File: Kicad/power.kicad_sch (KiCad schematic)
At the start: 22 parts, among them J6 350543-1, J7 22112042

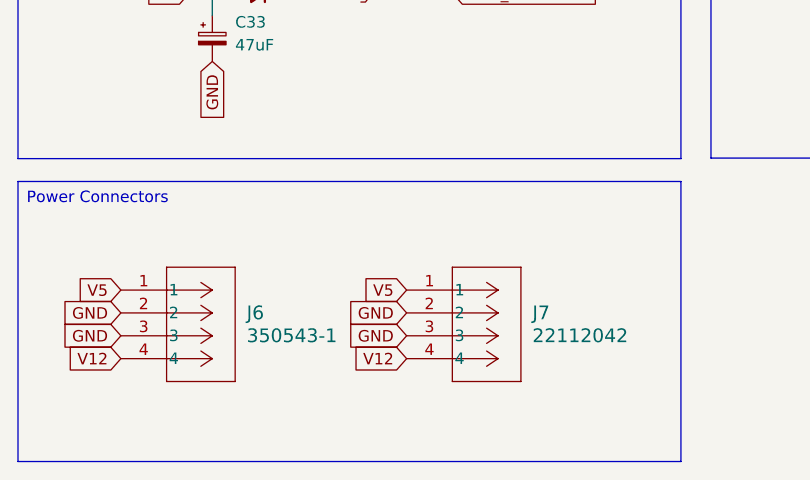
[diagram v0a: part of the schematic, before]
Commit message: Remove large Molex power connector
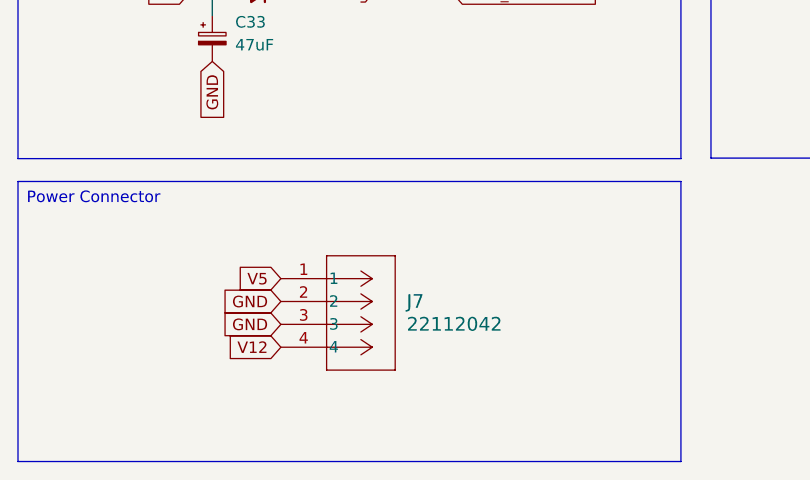
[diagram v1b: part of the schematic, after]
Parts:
- removed J6: 350543-1, 350543_1:CONN_350543-1_TYC, symbol 350543_1:350543-1
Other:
- moved on the sheet: J7
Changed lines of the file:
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@@
 		)
 	)
-	(text_box "Power Connectors\n"
+	(text_box "Power Connector\n"
 		(exclude_from_sim no)
 		(at 21.59 100.965 0)
@@
 		)
 	)
-	(global_label "V12"
-		(shape input)
-		(at 33.02 120.65 180)
-		(fields_autoplaced yes)
-		(effects
-			(font
-				(size 1.27 1.27)
-			)
-			(justify right)
-		)
-		(property "Intersheetrefs" "${INTERSHEET_REFS}"
-			(at 26.5272 120.65 0)
-			(effects
-				(font
-					(size 1.27 1.27)
-				)
-				(justify right)
-				(hide yes)
-			)
-		)
-	)
 	(global_label "GND"
 		(shape input)
@@
 	(global_label "V5"
 		(shape input)
-		(at 33.02 113.03 180)
-		(fields_autoplaced yes)
-		(effects
-			(font
-				(size 1.27 1.27)
-			)
-			(justify right)
-		)
-		(property "Intersheetrefs" "${INTERSHEET_REFS}"
-			(at 27.7367 113.03 0)
-			(effects
-				(font
-					(size 1.27 1.27)
-				)
-				(justify right)
-				(hide yes)
-			)
-		)
-	)
-	(global_label "V5"
-		(shape input)
 		(at 115.57 35.56 90)
 		(fields_autoplaced yes)
@@
 	(global_label "V5"
 		(shape input)
-		(at 64.77 113.03 180)
+		(at 50.8 111.76 180)
 		(fields_autoplaced yes)
 		(effects
@@
 		)
 		(property "Intersheetrefs" "${INTERSHEET_REFS}"
-			(at 59.4867 113.03 0)
+			(at 45.5167 111.76 0)
 			(effects
 				(font
@@
 	(global_label "GND"
 		(shape input)
-		(at 33.02 115.57 180)
-		(fields_autoplaced yes)
-		(effects
-			(font
-				(size 1.27 1.27)
-			)
-			(justify right)
-		)
-		(property "Intersheetrefs" "${INTERSHEET_REFS}"
-			(at 26.1643 115.57 0)
-			(effects
-				(font
-					(size 1.27 1.27)
-				)
-				(justify right)
-				(hide yes)
-			)
-		)
-	)
-	(global_label "GND"
-		(shape input)
 		(at 104.14 43.18 270)
 		(fields_autoplaced yes)
@@
 		(property "Intersheetrefs" "${INTERSHEET_REFS}"
 			(at 104.14 50.0357 90)
-			(effects
-				(font
-					(size 1.27 1.27)
-				)
-				(justify right)
-				(hide yes)
-			)
-		)
-	)
-	(global_label "GND"
-		(shape input)
-		(at 33.02 118.11 180)
-		(fields_autoplaced yes)
-		(effects
-			(font
-				(size 1.27 1.27)
-			)
-			(justify right)
-		)
-		(property "Intersheetrefs" "${INTERSHEET_REFS}"
-			(at 26.1643 118.11 0)
 			(effects
 				(font
@@
 	(global_label "GND"
 		(shape input)
-		(at 64.77 115.57 180)
+		(at 50.8 114.3 180)
 		(fields_autoplaced yes)
 		(effects
@@
 		)
 		(property "Intersheetrefs" "${INTERSHEET_REFS}"
-			(at 57.9143 115.57 0)
+			(at 43.9443 114.3 0)
 			(effects
 				(font
@@
 	(global_label "GND"
 		(shape input)
-		(at 64.77 118.11 180)
+		(at 50.8 116.84 180)
 		(fields_autoplaced yes)
 		(effects
@@
 		)
 		(property "Intersheetrefs" "${INTERSHEET_REFS}"
-			(at 57.9143 118.11 0)
+			(at 43.9443 116.84 0)
 			(effects
 				(font
@@
 	(global_label "V12"
 		(shape input)
-		(at 64.77 120.65 180)
+		(at 50.8 119.38 180)
 		(fields_autoplaced yes)
 		(effects
@@
 		)
 		(property "Intersheetrefs" "${INTERSHEET_REFS}"
-			(at 58.2772 120.65 0)
+			(at 44.3072 119.38 0)
 			(effects
 				(font
@@
 	)
 	(symbol
-		(lib_id "350543_1:350543-1")
-		(at 33.02 113.03 0)
-		(unit 1)
-		(exclude_from_sim no)
-		(in_bom yes)
-		(on_board yes)
-		(dnp no)
-		(fields_autoplaced yes)
-		(property "Reference" "J6"
-			(at 46.99 115.5699 0)
-			(effects
-				(font
-					(size 1.524 1.524)
-				)
-				(justify left)
-			)
-		)
-		(property "Value" "350543-1"
-			(at 46.99 118.1099 0)
-			(effects
-				(font
-					(size 1.524 1.524)
-				)
-				(justify left)
-			)
-		)
-		(property "Footprint" "350543_1:CONN_350543-1_TYC"
-			(at 33.02 113.03 0)
-			(effects
-				(font
-					(size 1.27 1.27)
-					(italic yes)
-				)
-				(hide yes)
-			)
-		)
-		(property "Datasheet" "350543-1"
-			(at 33.02 113.03 0)
-			(effects
-				(font
-					(size 1.27 1.27)
-					(italic yes)
-				)
-				(hide yes)
-			)
-		)
-		(property "Description" ""
-			(at 33.02 113.03 0)
-			(effects
-				(font
-					(size 1.27 1.27)
-				)
-				(hide yes)
-			)
-		)
-		(pin "4"
-		)
-		(pin "1"
-		)
-		(pin "2"
-		)
-		(pin "3"
-		)
-		(instances
-			(project ""
-				(path "/8f9f4021-47aa-41d9-bea7-f6ccf72098bb/166c366c-e5f9-4398-87d9-75fc4b57be99"
-					(reference "J6")
-					(unit 1)
-				)
-			)
-		)
-	)
-	(symbol
 		(lib_id "Device:C_Polarized_Small")
 		(at 104.14 40.64 0)
@@
 	(symbol
 		(lib_id "22112042:22112042")
-		(at 64.77 113.03 0)
+		(at 50.8 111.76 0)
 		(unit 1)
 		(exclude_from_sim no)
@@
 		(fields_autoplaced yes)
 		(property "Reference" "J7"
-			(at 78.74 115.5699 0)
+			(at 64.77 114.2999 0)
 			(effects
 				(font
@@
 		)
 		(property "Value" "22112042"
-			(at 78.74 118.1099 0)
+			(at 64.77 116.8399 0)
 			(effects
 				(font
@@
 		)
 		(property "Footprint" "22112042:CONN_A-6373-04A_MOL"
-			(at 64.77 113.03 0)
+			(at 50.8 111.76 0)
 			(effects
 				(font
@@
 		)
 		(property "Datasheet" "22112042"
-			(at 64.77 113.03 0)
+			(at 50.8 111.76 0)
 			(effects
 				(font
@@
 		)
 		(property "Description" ""
-			(at 64.77 113.03 0)
-			(effects
-				(font
+			(at 50.8 111.76 0)
+			(effects
+				(font

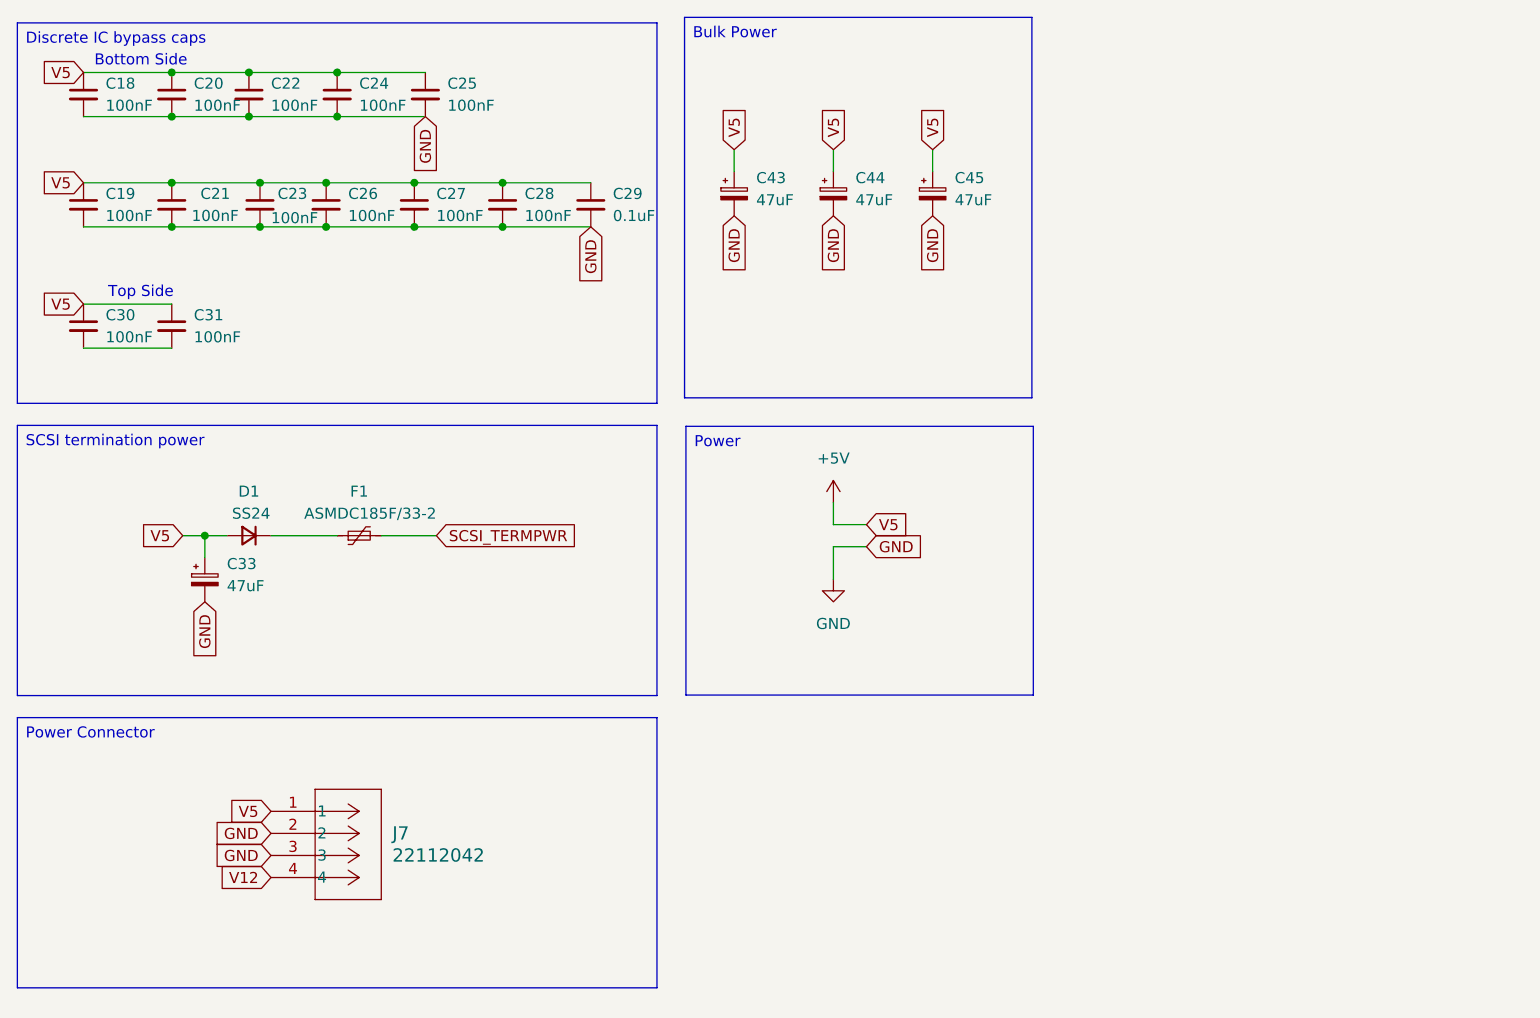
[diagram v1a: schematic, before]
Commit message: Fix various errors from issue #1
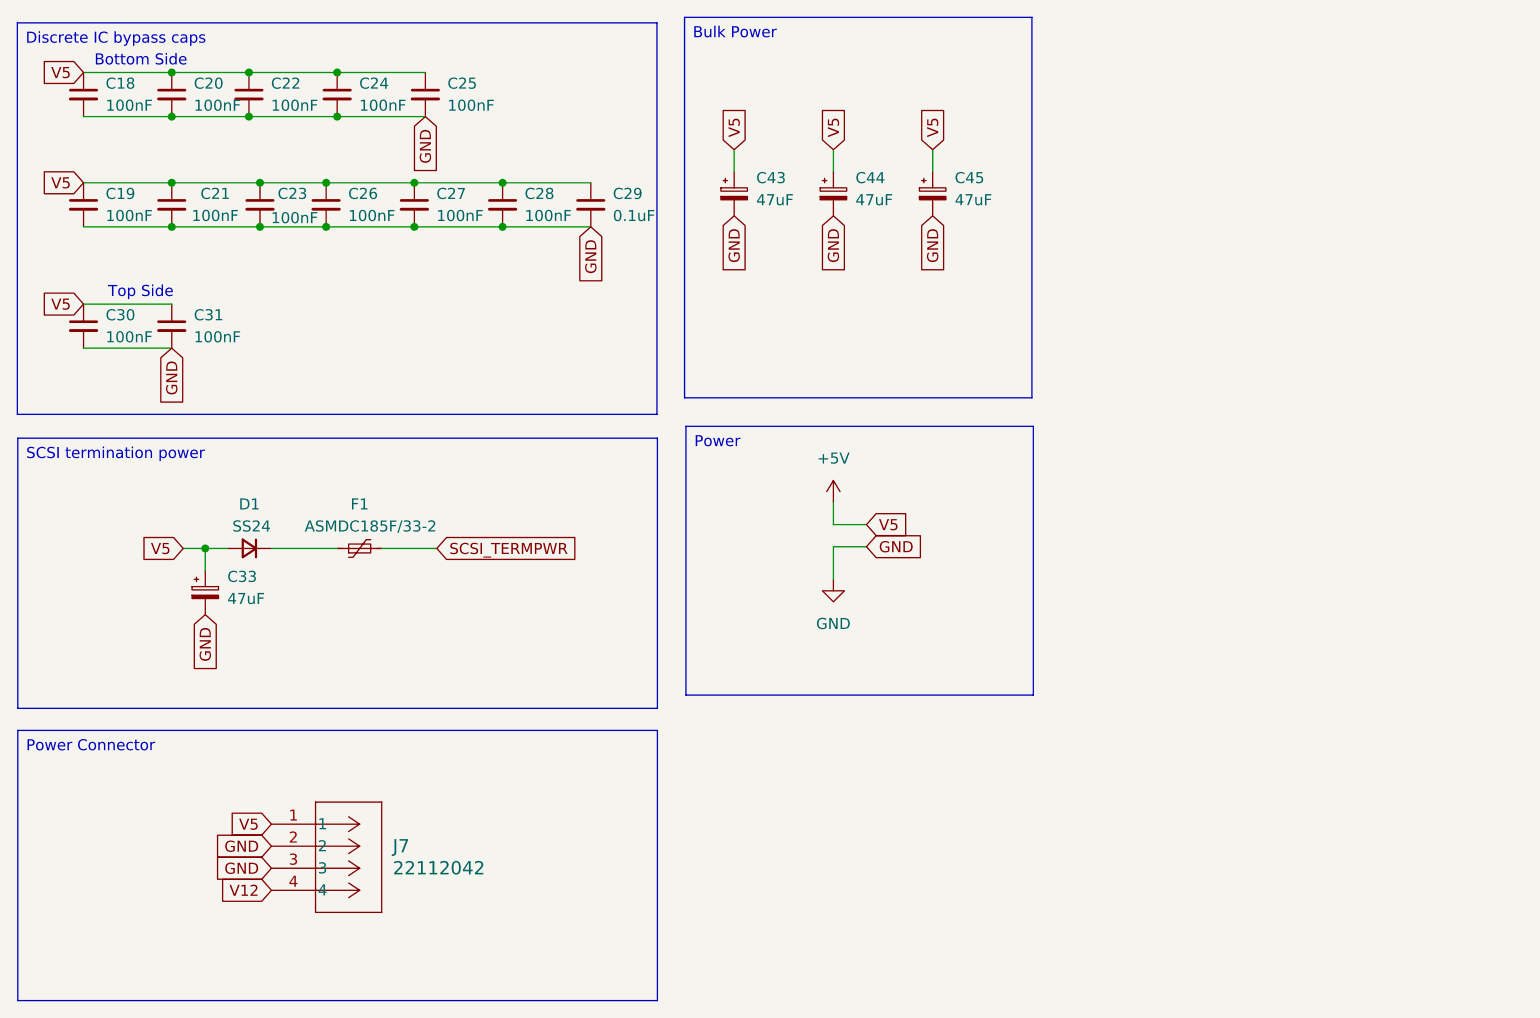
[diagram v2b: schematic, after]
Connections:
- net GND: now also C30.2, C31.2
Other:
- moved on the sheet: C33, D1, F1, J7
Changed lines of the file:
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@@
 	(text_box "SCSI termination power\n"
 		(exclude_from_sim no)
-		(at 21.59 67.31 0)
+		(at 21.6406 68.7843 0)
 		(size 73.66 31.115)
 		(margins 0.9525 0.9525 0.9525 0.9525)
@@
 	(text_box "Power Connector\n"
 		(exclude_from_sim no)
-		(at 21.59 100.965 0)
+		(at 21.6406 102.4393 0)
 		(size 73.66 31.115)
 		(margins 0.9525 0.9525 0.9525 0.9525)
@@
 		(exclude_from_sim no)
 		(at 21.59 20.955 0)
-		(size 73.66 43.815)
+		(size 73.66 45.085)
 		(margins 0.9525 0.9525 0.9525 0.9525)
 		(stroke
@@
 	)
 	(junction
-		(at 43.18 80.01)
+		(at 43.2306 81.4843)
 		(diameter 0)
 		(color 0 0 0 0)
@@
 	(wire
 		(pts
-			(xy 45.72 80.01) (xy 43.18 80.01)
+			(xy 45.7706 81.4843) (xy 43.2306 81.4843)
 		)
 		(stroke
@@
 	(wire
 		(pts
-			(xy 69.85 80.01) (xy 63.5 80.01)
-		)
-		(stroke
-			(width 0)
-			(type default)
-		)
-	)
-	(wire
-		(pts
-			(xy 43.18 80.01) (xy 43.18 82.55)
+			(xy 69.9006 81.4843) (xy 63.5506 81.4843)
+		)
+		(stroke
+			(width 0)
+			(type default)
+		)
+	)
+	(wire
+		(pts
+			(xy 43.2306 81.4843) (xy 43.2306 84.0243)
 		)
 		(stroke
@@
 	(wire
 		(pts
-			(xy 40.64 80.01) (xy 43.18 80.01)
-		)
-		(stroke
-			(width 0)
-			(type default)
-		)
-	)
-	(wire
-		(pts
-			(xy 58.42 80.01) (xy 50.8 80.01)
+			(xy 40.6906 81.4843) (xy 43.2306 81.4843)
+		)
+		(stroke
+			(width 0)
+			(type default)
+		)
+	)
+	(wire
+		(pts
+			(xy 58.4706 81.4843) (xy 50.8506 81.4843)
 		)
 		(stroke
@@
 	(global_label "SCSI_TERMPWR"
 		(shape input)
-		(at 69.85 80.01 0)
+		(at 69.9006 81.4843 0)
 		(fields_autoplaced yes)
 		(effects
@@
 		)
 		(property "Intersheetrefs" "${INTERSHEET_REFS}"
-			(at 86.926 80.01 0)
+			(at 86.9766 81.4843 0)
 			(effects
 				(font
@@
 	(global_label "V5"
 		(shape input)
-		(at 50.8 111.76 180)
+		(at 50.8506 113.2343 180)
 		(fields_autoplaced yes)
 		(effects
@@
 		)
 		(property "Intersheetrefs" "${INTERSHEET_REFS}"
-			(at 45.5167 111.76 0)
+			(at 45.5673 113.2343 0)
 			(effects
 				(font
@@
 	(global_label "GND"
 		(shape input)
-		(at 43.18 87.63 270)
+		(at 43.2306 89.1043 270)
 		(fields_autoplaced yes)
 		(effects
@@
 		)
 		(property "Intersheetrefs" "${INTERSHEET_REFS}"
-			(at 43.18 94.4857 90)
+			(at 43.2306 95.96 90)
 			(effects
 				(font
@@
 	(global_label "GND"
 		(shape input)
-		(at 50.8 114.3 180)
+		(at 50.8506 115.7743 180)
 		(fields_autoplaced yes)
 		(effects
@@
 		)
 		(property "Intersheetrefs" "${INTERSHEET_REFS}"
-			(at 43.9443 114.3 0)
+			(at 43.9949 115.7743 0)
 			(effects
 				(font
@@
 	(global_label "V5"
 		(shape input)
-		(at 40.64 80.01 180)
+		(at 40.6906 81.4843 180)
 		(fields_autoplaced yes)
 		(effects
@@
 		)
 		(property "Intersheetrefs" "${INTERSHEET_REFS}"
-			(at 35.3567 80.01 0)
+			(at 35.4073 81.4843 0)
 			(effects
 				(font
@@
 	(global_label "GND"
 		(shape input)
-		(at 50.8 116.84 180)
+		(at 50.8506 118.3143 180)
 		(fields_autoplaced yes)
 		(effects
@@
 		)
 		(property "Intersheetrefs" "${INTERSHEET_REFS}"
-			(at 43.9443 116.84 0)
+			(at 43.9949 118.3143 0)
 			(effects
 				(font
@@
 	(global_label "V12"
 		(shape input)
-		(at 50.8 119.38 180)
+		(at 50.8506 120.8543 180)
 		(fields_autoplaced yes)
 		(effects
@@
 		)
 		(property "Intersheetrefs" "${INTERSHEET_REFS}"
-			(at 44.3072 119.38 0)
+			(at 44.3578 120.8543 0)
+			(effects
+				(font
+					(size 1.27 1.27)
+				)
+				(justify right)
+				(hide yes)
+			)
+		)
+	)
+	(global_label "GND"
+		(shape input)
+		(at 39.37 58.42 270)
+		(fields_autoplaced yes)
+		(effects
+			(font
+				(size 1.27 1.27)
+			)
+			(justify right)
+		)
+		(property "Intersheetrefs" "${INTERSHEET_REFS}"
+			(at 39.37 65.2757 90)
 			(effects
 				(font
@@
 	(symbol
 		(lib_id "Device:Polyfuse_Small")
-		(at 60.96 80.01 90)
+		(at 61.0106 81.4843 90)
 		(unit 1)
 		(exclude_from_sim no)
@@
 		(dnp no)
 		(property "Reference" "F1"
-			(at 60.96 74.93 90)
+			(at 61.0106 76.4043 90)
 			(effects
 				(font
@@
 		)
 		(property "Value" "ASMDC185F/33-2"
-			(at 62.23 77.47 90)
+			(at 62.2806 78.9443 90)
 			(effects
 				(font
@@
 		)
 		(property "Footprint" "Fuse:Fuse_2920_7451Metric_Pad2.10x5.45mm_HandSolder"
-			(at 66.04 78.74 0)
+			(at 66.0906 80.2143 0)
 			(effects
 				(font
@@
 		)
 		(property "Datasheet" "~"
-			(at 60.96 80.01 0)
+			(at 61.0106 81.4843 0)
 			(effects
 				(font
@@
 		)
 		(property "Description" "Resettable fuse, polymeric positive temperature coefficient, small symbol"
-			(at 60.96 80.01 0)
+			(at 61.0106 81.4843 0)
 			(effects
 				(font
@@
 	(symbol
 		(lib_id "22112042:22112042")
-		(at 50.8 111.76 0)
+		(at 50.8506 113.2343 0)
 		(unit 1)
 		(exclude_from_sim no)
@@
 		(fields_autoplaced yes)
 		(property "Reference" "J7"
-			(at 64.77 114.2999 0)
+			(at 64.8206 115.7742 0)
 			(effects
 				(font
@@
 		)
 		(property "Value" "22112042"
-			(at 64.77 116.8399 0)
+			(at 64.8206 118.3142 0)
 			(effects
 				(font
@@
 		)
 		(property "Footprint" "22112042:CONN_A-6373-04A_MOL"
-			(at 50.8 111.76 0)
+			(at 50.8506 113.2343 0)
 			(effects
 				(font
@@
 		)
 		(property "Datasheet" "22112042"
-			(at 50.8 111.76 0)
+			(at 50.8506 113.2343 0)
 			(effects
 				(font
@@
 		)
 		(property "Description" ""
-			(at 50.8 111.76 0)
+			(at 50.8506 113.2343 0)
 			(effects
 				(font
@@
 	(symbol
 		(lib_id "Device:D_Small")
-		(at 48.26 80.01 180)
+		(at 48.3106 81.4843 180)
 		(unit 1)
 		(exclude_from_sim no)
@@
 		(dnp no)
 		(property "Reference" "D1"
-			(at 48.26 74.93 0)
+			(at 48.3106 76.4043 0)
 			(effects
 				(font
@@
 		)
 		(property "Value" "SS24"
-			(at 48.514 77.47 0)
+			(at 48.5646 78.9443 0)
 			(effects
 				(font
@@
 		)
 		(property "Footprint" "Diode_SMD:D_SMA_Handsoldering"
-			(at 48.26 80.01 90)
+			(at 48.3106 81.4843 90)
 			(effects
 				(font
@@
 		)
 		(property "Datasheet" "https://www.onsemi.com/pdf/datasheet/mbr140sft1-d.pdf"
-			(at 48.26 80.01 90)
+			(at 48.3106 81.4843 90)
 			(effects
 				(font
@@
 		)
 		(property "Description" "Diode, small symbol"
-			(at 48.26 80.01 0)
+			(at 48.3106 81.4843 0)
 			(effects
 				(font
@@
 		)
 		(property "Sim.Device" "D"
-			(at 48.26 80.01 0)
+			(at 48.3106 81.4843 0)
 			(effects
 				(font
@@
 		)
 		(property "Sim.Pins" "1=K 2=A"
-			(at 48.26 80.01 0)
+			(at 48.3106 81.4843 0)
 			(effects
 				(font
@@
 	(symbol
 		(lib_id "Device:C_Polarized_Small")
-		(at 43.18 85.09 0)
+		(at 43.2306 86.5643 0)
 		(unit 1)
 		(exclude_from_sim no)
@@
 		(fields_autoplaced yes)
 		(property "Reference" "C33"
-			(at 45.72 83.2738 0)
+			(at 45.7706 84.7481 0)
 			(effects
 				(font
@@
 		)
 		(property "Value" "47uF"
-			(at 45.72 85.8138 0)
+			(at 45.7706 87.2881 0)
 			(effects
 				(font
@@
 		)
 		(property "Footprint" "Capacitor_SMD:CP_Elec_6.3x7.7"
-			(at 43.18 85.09 0)
+			(at 43.2306 86.5643 0)
 			(effects
 				(font
@@
 		)
 		(property "Datasheet" "~"
-			(at 43.18 85.09 0)
+			(at 43.2306 86.5643 0)
 			(effects
 				(font
@@
 		)
 		(property "Description" "Polarized capacitor, small symbol"
-			(at 43.18 85.09 0)
-			(effects
-				(font
+			(at 43.2306 86.5643 0)
+			(effects
+				(font

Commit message: Update sheet, add pull down on ROM_CE
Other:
- company: (none) -> amiga.technology
- title: (none) -> A4092
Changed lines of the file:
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@@
 	(generator_version "9.0")
 	(paper "A4")
+	(title_block
+		(title "A4092")
+		(rev "PROTO0")
+		(company "amiga.technology")
+	)
 	(text "Bottom Side\n"
 		(exclude_from_sim no)

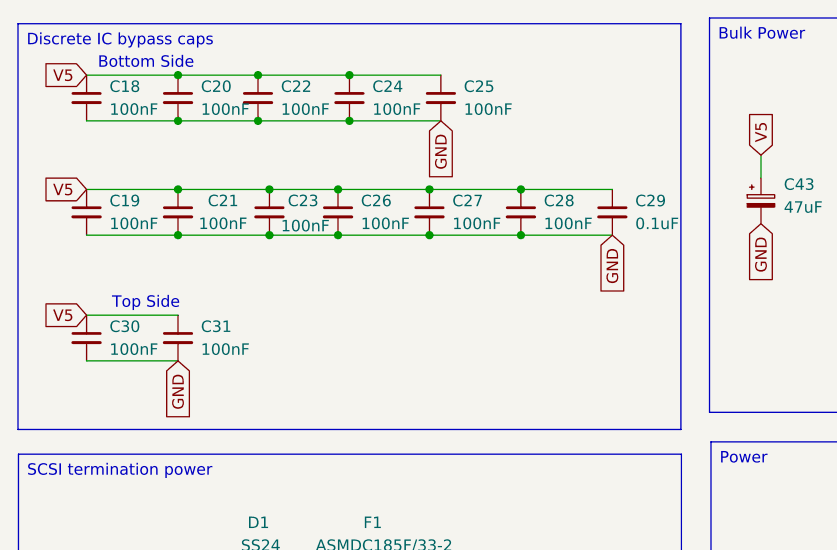
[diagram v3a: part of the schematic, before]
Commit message: Rename majority of bypass capacitors to match their Uxx
i.e. U4 will have C4A, C4B, C4C, C4D
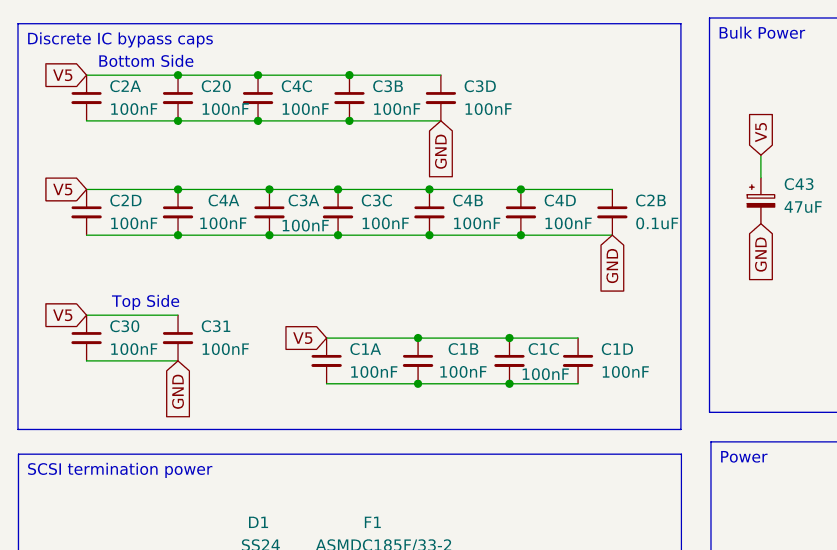
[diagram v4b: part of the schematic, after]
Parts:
- added C1A, C1B, C1C, C1D: 100nF, Capacitor_SMD:C_0603_1608Metric_Pad1.08x0.95mm_HandSolder, symbol Device:C_Small
- renumbered C18 to C2A, C29 to C2B, C19 to C2D, C23 to C3A, C24 to C3B, C26 to C3C, C25 to C3D, C21 to C4A, C27 to C4B, C22 to C4C, C28 to C4D
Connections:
- net +5V: now also C1A.1, C1B.1, C1C.1, C1D.1
- new net: C1A.2, C1B.2, C1C.2, C1D.2
